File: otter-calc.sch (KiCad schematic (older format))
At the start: 0 parts

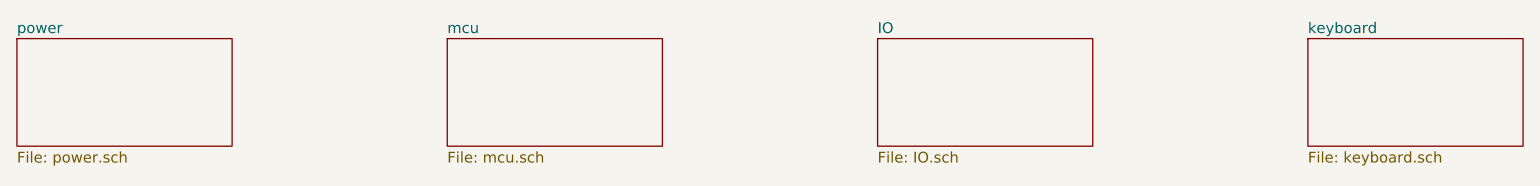
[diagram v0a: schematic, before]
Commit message: Reduce to two sheets
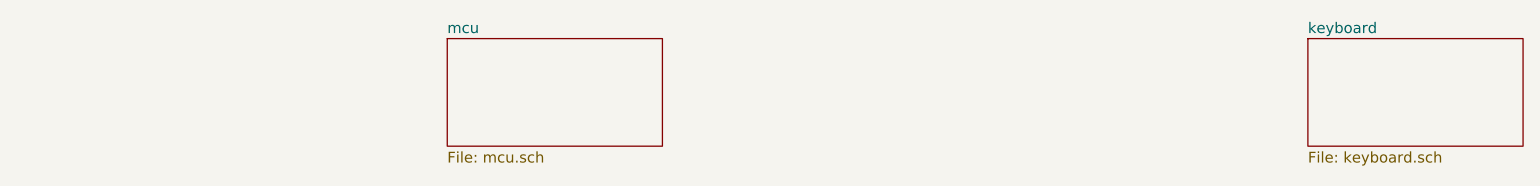
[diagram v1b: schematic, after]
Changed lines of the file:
@@
 $EndDescr
-$Sheet
-S 1500 2000 1000 500
-U 5F7C2971
-F0 "power" 50
-F1 "power.sch" 50
-$EndSheet
 $Sheet
 S 3500 2000 1000 500
@@
 $EndSheet
 $Sheet
-S 5500 2000 1000 500
-U 5F7C2A19
-F0 "IO" 50
-F1 "IO.sch" 50
-$EndSheet
-$Sheet

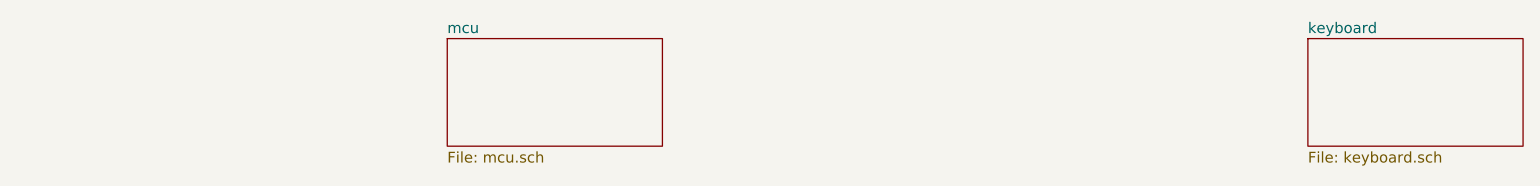
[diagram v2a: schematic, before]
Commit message: Add a datasheet; Split power into own schematic
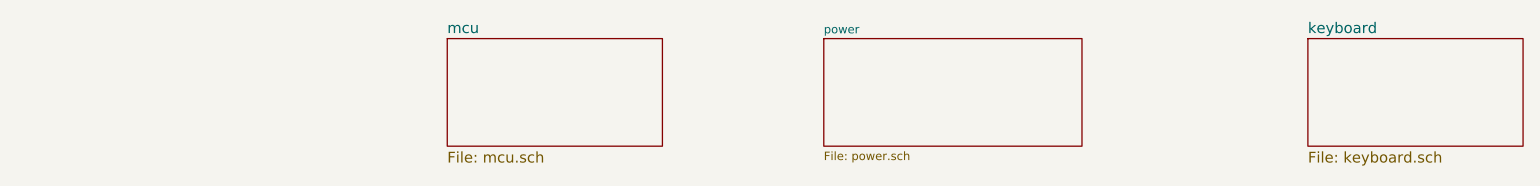
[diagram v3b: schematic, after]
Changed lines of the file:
@@
 $Descr A4 11693 8268
 encoding utf-8
-Sheet 1 3
+Sheet 1 4
 Title ""
 Date ""
@@
 F1 "keyboard.sch" 50
 $EndSheet
+$Sheet
+S 5250 2000 1200 500
+U 60CFD8F5
+F0 "power" 39
+F1 "power.sch" 39
+$EndSheet
 $EndSCHEMATC
